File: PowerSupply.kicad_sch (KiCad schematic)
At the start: 17 parts, among them U3 nPM1100-CAXX, U6 TPS62173DSG, U9 TPS22917DBV

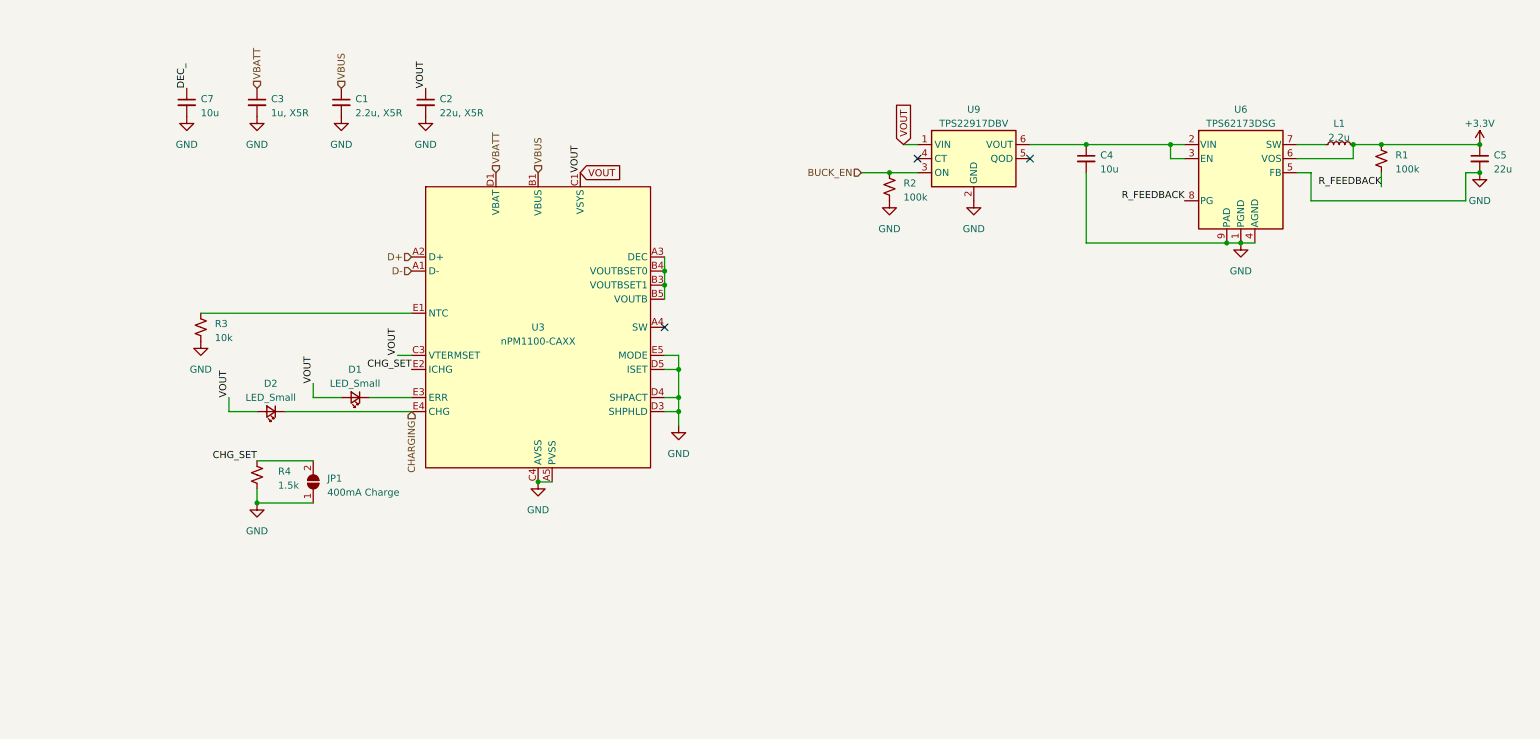
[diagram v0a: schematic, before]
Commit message: Added passvies and bus connections to nRF7002
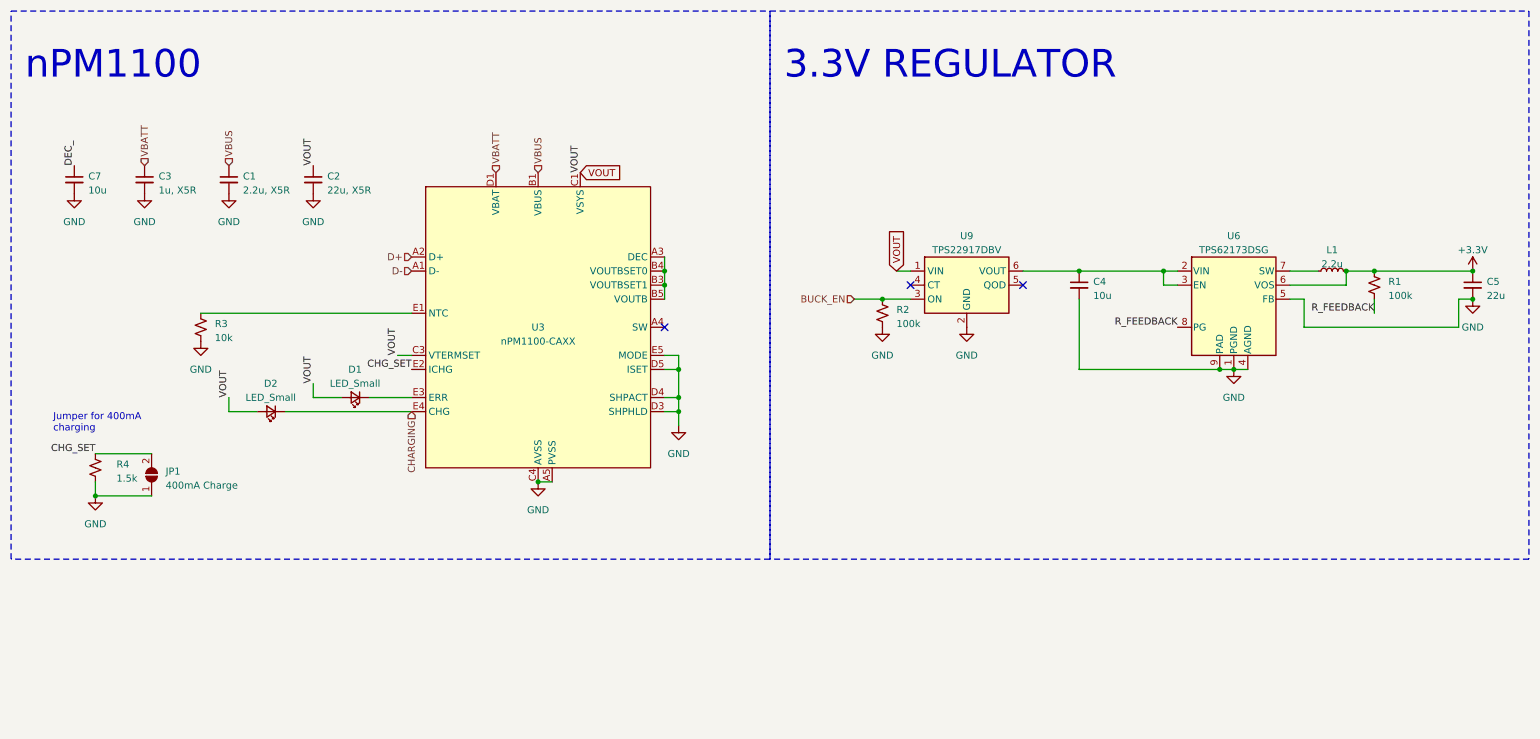
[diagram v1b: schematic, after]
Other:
- note added: "3.3V REGULATOR"
- note added: "Jumper for 400mA charging"
- note added: "nPM1100"
- moved on the sheet: C1, C2, C3, C4, C5, C7, JP1, L1, R1, R2, R4, U6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

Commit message: Schematic complete.
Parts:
- removed D1, D2: LED_Small, symbol Device:LED_Small
- removed JP1: 400mA Charge, Jumper:SolderJumper-2_P1.3mm_Open_RoundedPad1.0x1.5mm, symbol Jumper:SolderJumper_2_Open
- removed R3: 10k, symbol Device:R_Small_US
- removed R4: 1.5k, symbol Device:R_Small_US
- removed U3: nPM1100-CAXX, nordic-lib-kicad-npm:BGA-25_5x5_2.075x2.075mm, symbol nordic-lib-kicad-npm:nPM1100-CAXX
- removed U6: TPS62173DSG, Package_SON:WSON-8-1EP_2x2mm_P0.5mm_EP0.9x1.6mm_ThermalVias, symbol Regulator_Switching:TPS62173DSG
- removed U9: TPS22917DBV, Package_TO_SOT_SMD:SOT-23-6, symbol Power_Management:TPS22917DBV
- added C57: 10u, Capacitor_SMD:C_0402_1005Metric, symbol Device:C_Small
- added C58: 100n, Capacitor_SMD:C_0402_1005Metric, symbol Device:C_Small
- added C59: 1u, Capacitor_SMD:C_0402_1005Metric, symbol Device:C_Small
- added D1: LED_ARGB, LED_SMD:LED_SK6812_EC15_1.5x1.5mm, symbol Device:LED_ARGB
- added L6: 2.2u, Inductor_SMD:L_0805_2012Metric, symbol Device:L_Small
- added U3: nPM1300-QEXX, Package_DFN_QFN:QFN-32-1EP_5x5mm_P0.5mm_EP3.6x3.6mm_ThermalVias, symbol nordic-lib-kicad-npm:nPM1300-QEXX
- C1: value 2.2u, X5R -> 10u; footprint (none) -> Capacitor_SMD:C_0402_1005Metric
- C2: value 22u, X5R -> 10u; footprint (none) -> Capacitor_SMD:C_0402_1005Metric
- C3: value 1u, X5R -> 2.2u; footprint (none) -> Capacitor_SMD:C_0402_1005Metric
- C4: value 10u -> 1u; footprint (none) -> Capacitor_SMD:C_0402_1005Metric
- C5: value 22u -> 10u; footprint (none) -> Capacitor_SMD:C_0402_1005Metric
- C7: footprint (none) -> Capacitor_SMD:C_0402_1005Metric
- L1: footprint (none) -> Inductor_SMD:L_0805_2012Metric
- R1: value 100k -> 47k; footprint (none) -> Resistor_SMD:R_0603_1608Metric
- R2: value 100k -> 360k; footprint (none) -> Resistor_SMD:R_0603_1608Metric
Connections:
- net R_FEEDBACK is gone; now on net GND: R1.2
- net VBUS is gone; now on net +1V8: C1.1
- net GND: now also C57.2, C58.2, C59.2, U3.18 (NTC), U3.2 (PVSS1), U3.33 (AVSS), U3.6 (PVSS2)
- net VBUS_IN: now reaches C4.1
- net VBUS_IN: now also U3.21 (VBUS)
- net +1V8: now reaches L1.1
- net +1V8: now also U3.1 (VOUT1)
- removed net +3.3V: C5.1, L1.2, R1.1
- net BUCK_EN: no longer names the net of R2.1
- net BUCK_EN: now also U3.16 (VSET2)
- net DEC_ renamed VSYS
- net VSYS: now also C5.1, C57.1, D1.1 (A), U3.20 (VSYS), U3.4 (PVDD)
- net VBATT renamed VBAT
- net VBAT: now also U3.19 (VBAT)
- net VOUT renamed +3V3
- net +3V3: now also C58.1, L6.1, U3.12 (VDDIO), U3.32 (VOUT2)
- new net: R1.1, U3.17 (VSET1)
- new net: D1.2 (RK), U3.25 (LED0)
- new net: D1.3 (GK), U3.26 (LED1)
- new net: D1.4 (BK), U3.27 (LED2)
- new net: L1.2, U3.3 (SW1)
- new net: L6.2, U3.5 (SW2)
- new net CC1: U3.23 (CC1)
- new net CC2: U3.24 (CC2)
- new net LSIN1: U3.28 (LSIN1/VINLDO1)
- new net LSIN2: U3.30 (LSIN2/VINLDO2)
- new net LSOUT1: U3.29 (LSOUT1/VOUTLDO1)
- new net LSOUT2: U3.31 (LSOUT2/VOUTLDO2)
- new net NPM_SCL: U3.14 (SCL)
- new net NPM_SDA: U3.13 (SDA)
- new net REG_EN: U3.7 (GPIO0)
- new net SHPHLD: U3.15 (SHPHLD)
- new net VBUS_OUT: C59.1, U3.22 (VBUSOUT)
- no-connect marks 3 -> 4
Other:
- note added: "360K = 3.3V on VSET2"
- note added: "47K = 1.8V on VSET1"
- note removed: "3.3V REGULATOR"
- note removed: "Jumper for 400mA charging"
- note removed: "nPM1100"
